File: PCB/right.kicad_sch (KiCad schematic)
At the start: 112 parts, among them SW1 SW_Push, SW10 SW_Push, SW11 SW_Push, SW12 SW_Push, SW13 SW_Push, SW14 SW_Push, SW15 SW_Push, SW16 SW_Push, SW17 SW_Push, SW18 SW_Push, SW19 SW_Push, SW2 SW_Push, SW20 SW_Push, SW21 SW_Push, SW22 SW_Push, SW23 SW_Push, SW24 SW_Push, SW25 SW_Push, SW26 SW_Push, SW27 SW_Push, SW28 SW_Push, SW29 SW_Push, SW3 SW_Push, SW30 SW_Push, SW31 SW_Push, SW32 SW_Push, SW33 SW_Push, SW34 SW_Push, SW35 SW_Push, SW36 SW_Push, SW37 SW_Push, SW38 SW_Push, SW39 SW_Push, SW4 SW_Push, SW40 SW_Push, SW41 SW_Push, SW42 SW_Push, SW43 SW_Push, SW44 SW_Push, SW45 SW_Push, SW46 SW_Push, SW47 SW_Push, SW48 SW_Push, SW49 SW_Push, SW5 SW_Push, SW50 SW_Push, SW51 SW_Push, SW52 SW_Push, SW53 SW_Push, SW54 SW_Push, SW55 SW_Push, SW6 SW_Push, SW7 SW_Push, SW8 SW_Push, SW9 SW_Push, U2 MCP23017_SO

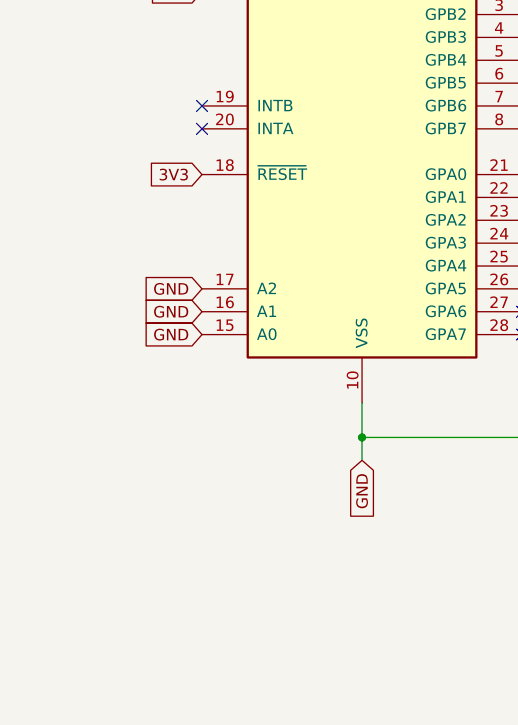
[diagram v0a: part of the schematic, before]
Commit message: Added all files required for the display based keyboard
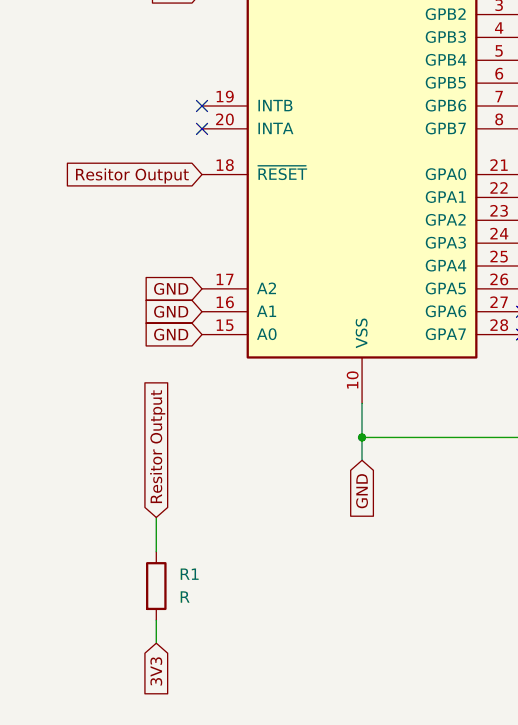
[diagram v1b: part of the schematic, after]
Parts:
- added R1: R, symbol Device:R
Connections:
- net 3V3: now also R1.2; no longer U2.18 (~{RESET})
- new net Resitor Output: R1.1, U2.18 (~{RESET})
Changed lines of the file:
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@@
 	(wire
 		(pts
+			(xy 26.67 137.16) (xy 26.67 139.7)
+		)
+		(stroke
+			(width 0)
+			(type default)
+		)
+	)
+	(wire
+		(pts
 			(xy 200.66 82.55) (xy 213.36 82.55)
 		)
@@
 	(wire
 		(pts
+			(xy 26.67 125.73) (xy 26.67 129.54)
+		)
+		(stroke
+			(width 0)
+			(type default)
+		)
+	)
+	(wire
+		(pts
 			(xy 190.5 74.93) (xy 190.5 87.63)
 		)
@@
 		)
 	)
+	(global_label "Resitor Output"
+		(shape input)
+		(at 26.67 125.73 90)
+		(fields_autoplaced yes)
+		(effects
+			(font
+				(size 1.27 1.27)
+			)
+			(justify left)
+		)
+		(property "Intersheetrefs" "${INTERSHEET_REFS}"
+			(at 26.67 108.8959 90)
+			(effects
+				(font
+					(size 1.27 1.27)
+				)
+				(justify left)
+				(hide yes)
+			)
+		)
+	)
 	(global_label "Col 6"
 		(shape input)
@@
 		)
 	)
+	(global_label "3V3"
+		(shape input)
+		(at 26.67 139.7 270)
+		(fields_autoplaced yes)
+		(effects
+			(font
+				(size 1.27 1.27)
+			)
+			(justify right)
+		)
+		(property "Intersheetrefs" "${INTERSHEET_REFS}"
+			(at 26.67 146.1928 90)
+			(effects
+				(font
+					(size 1.27 1.27)
+				)
+				(justify right)
+				(hide yes)
+			)
+		)
+	)
 	(global_label "Col 2"
 		(shape input)
@@
 		)
 	)
-	(global_label "Col 13"
+	(global_label "Resitor Output"
 		(shape input)
-		(at 67.31 90.17 0)
+		(at 31.75 87.63 180)
 		(fields_autoplaced yes)
 		(effects
@@
 				(size 1.27 1.27)
 			)
-			(justify left)
+			(justify right)
 		)
 		(property "Intersheetrefs" "${INTERSHEET_REFS}"
-			(at 76.766 90.17 0)
+			(at 14.9159 87.63 0)
 			(effects
 				(font
 					(size 1.27 1.27)
 				)
-				(justify left)
+				(justify right)
 				(hide yes)
 			)
 		)
 	)
-	(global_label "Col 14"
+	(global_label "Col 13"
 		(shape input)
-		(at 67.31 92.71 0)
+		(at 67.31 90.17 0)
 		(fields_autoplaced yes)
 		(effects
@@
 		)
 		(property "Intersheetrefs" "${INTERSHEET_REFS}"
-			(at 76.766 92.71 0)
+			(at 76.766 90.17 0)
 			(effects
 				(font
@@
 		)
 	)
-	(global_label "Row 5"
+	(global_label "Col 14"
 		(shape input)
-		(at 127 107.95 180)
+		(at 67.31 92.71 0)
 		(fields_autoplaced yes)
 		(effects
@@
 				(size 1.27 1.27)
 			)
-			(justify right)
+			(justify left)
 		)
 		(property "Intersheetrefs" "${INTERSHEET_REFS}"
-			(at 118.0882 107.95 0)
+			(at 76.766 92.71 0)
 			(effects
 				(font
 					(size 1.27 1.27)
 				)
-				(justify right)
+				(justify left)
 				(hide yes)
 			)
 		)
 	)
-	(global_label "Row 4"
+	(global_label "Row 5"
 		(shape input)
-		(at 127 95.25 180)
+		(at 127 107.95 180)
 		(fields_autoplaced yes)
 		(effects
@@
 		)
 		(property "Intersheetrefs" "${INTERSHEET_REFS}"
-			(at 118.0882 95.25 0)
+			(at 118.0882 107.95 0)
 			(effects
 				(font
@@
 		)
 	)
-	(global_label "3V3"
+	(global_label "Row 4"
 		(shape input)
-		(at 31.75 87.63 180)
+		(at 127 95.25 180)
 		(fields_autoplaced yes)
 		(effects
@@
 		)
 		(property "Intersheetrefs" "${INTERSHEET_REFS}"
-			(at 25.2572 87.63 0)
+			(at 118.0882 95.25 0)
 			(effects
 				(font
@@
 					(unit 1)
 				)
+			)
+		)
+	)
+	(symbol
+		(lib_id "Device:R")
+		(at 26.67 133.35 0)
+		(unit 1)
+		(exclude_from_sim no)
+		(in_bom yes)
+		(on_board yes)
+		(dnp no)
+		(fields_autoplaced yes)
+		(property "Reference" "R1"
+			(at 29.21 132.0799 0)
+			(effects
+				(font
+					(size 1.27 1.27)
+				)
+				(justify left)
+			)
+		)
+		(property "Value" "R"
+			(at 29.21 134.6199 0)
+			(effects
+				(font
+					(size 1.27 1.27)
+				)
+				(justify left)
+			)
+		)
+		(property "Footprint" ""
+			(at 24.892 133.35 90)
+			(effects
+				(font
+					(size 1.27 1.27)
+				)
+				(hide yes)
+			)
+		)
+		(property "Datasheet" "~"
+			(at 26.67 133.35 0)
+			(effects
+				(font
+					(size 1.27 1.27)
+				)
+				(hide yes)
+			)
+		)
+		(property "Description" "Resistor"
+			(at 26.67 133.35 0)
+			(effects
+				(font
+					(size 1.27 1.27)
+				)
+				(hide yes)
+			)
+		)
+		(pin "1"
+		)
+		(pin "2"
+		)
+		(instances
+			(project ""
+				(path "/426f728c-d93c-40eb-b5f2-091f443adbca/fdcbd120-1d4a-47bd-be35-d0401c54bbb0"
+					(reference "R1")
+					(unit 1)
+				)
